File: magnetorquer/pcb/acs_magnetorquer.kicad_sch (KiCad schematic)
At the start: 14 parts, among them J1 Conn_01x02, J2 Conn_01x02, U1 L293

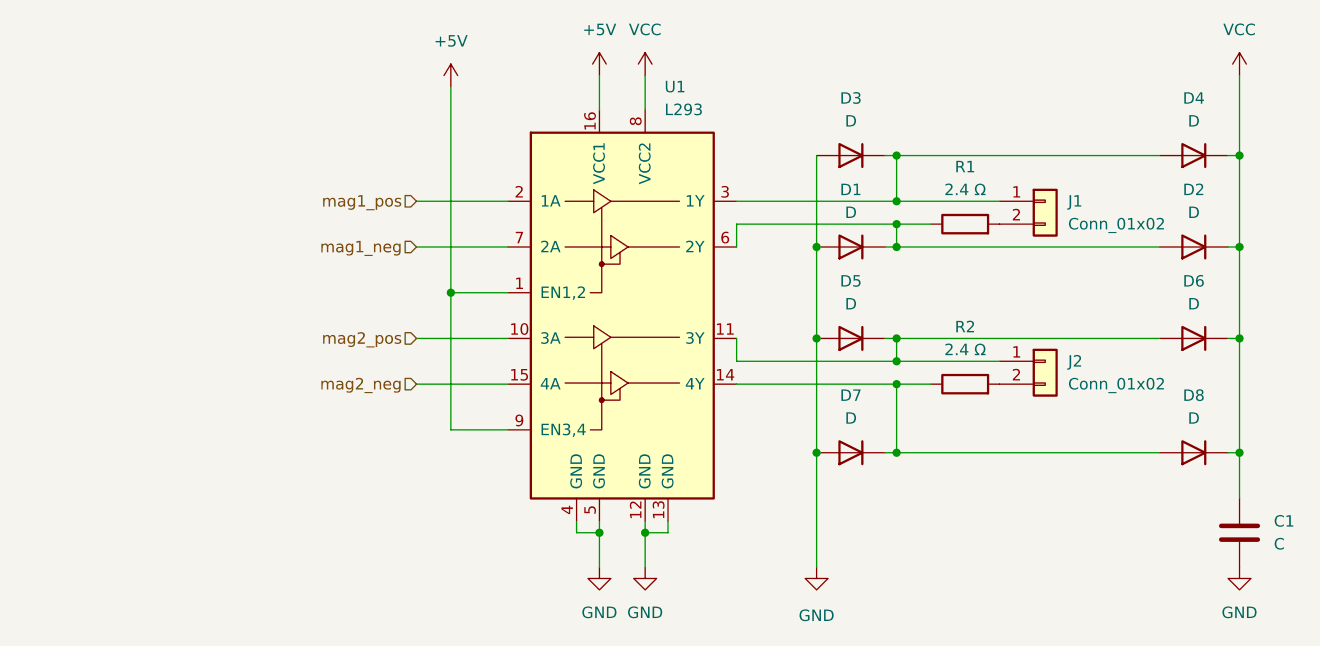
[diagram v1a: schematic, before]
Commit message: start routing pcb
It needs a power regulator and a battery terminal
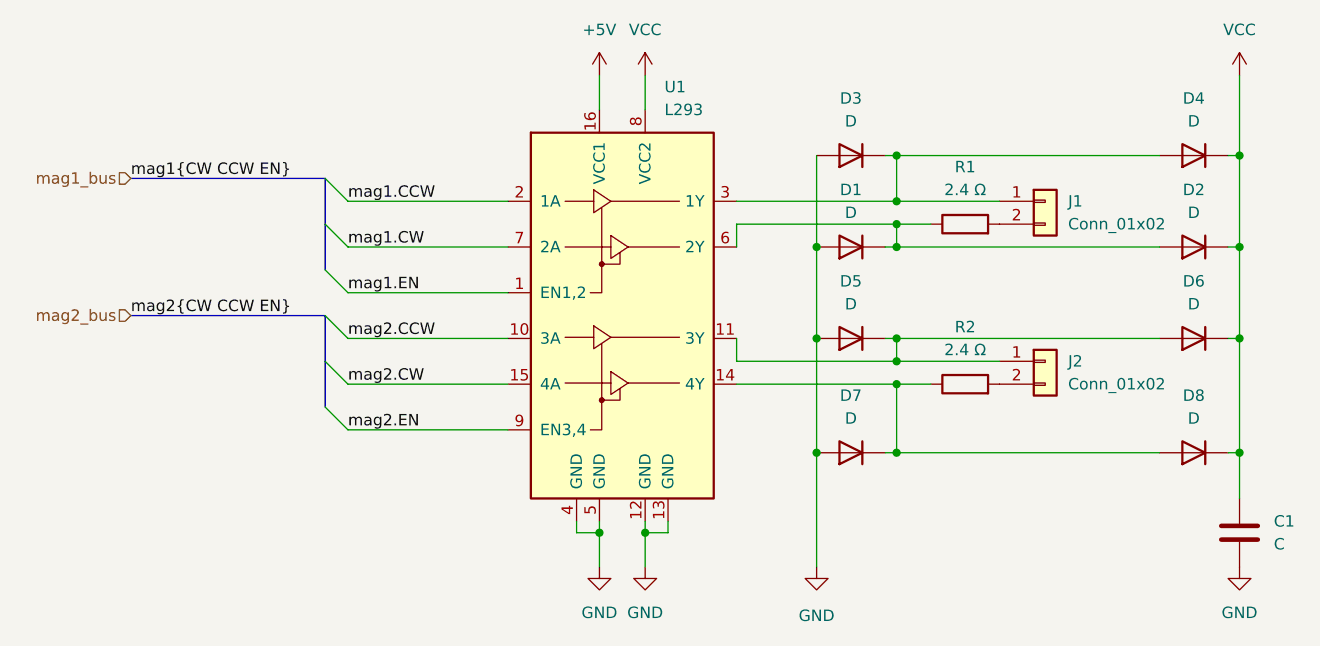
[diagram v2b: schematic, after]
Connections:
- net +5V: no longer U1.1 (EN1,2), U1.9 (EN3,4)
- net mag1_neg renamed mag1.CW
- net mag1_pos renamed mag1.CCW
- net mag2_neg renamed mag2.CW
- net mag2_pos renamed mag2.CCW
- new net mag1.EN: U1.1 (EN1,2)
- new net mag2.EN: U1.9 (EN3,4)
